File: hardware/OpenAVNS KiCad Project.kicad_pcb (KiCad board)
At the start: 4 copper layers, 69.9 x 100.9 mm, 210 parts, among them J1 Conn_ARM_JTAG_SWD_10, J2 AudioPlug3, J3 USB_C_Receptacle, J4 Conn_01x02_Pin, J5 Conn_01x03_Pin, Q1 BCV62, Q2 BC847, Q3 BC857, Q4 BCV61, Q5 BCV62, Q6 BC847, Q7 BC857, Q8 BCV61, SW1 SW_SPDT, T1 Wurth 750315839 - 1:10, 40uH, U1 TS5A3159AYZPR, U10 TLV9062, U11 LIS2DH12, U12 OPA455, U13 74AUC1G74, U14 TPS61200DRC, U15 LT1615ES5_TRPBF, U16 LT8304IS8E_PBF, U17 MCP73831-2-OT, U2 TLV9004xRUCR, U3 MCP4725xxx-xCH, U4 TS5A3159AYZPR, U5 nRF52840, U6 TS5A3159AYZPR, U7 MCP4725xxx-xCH, U8 TS5A3159AYZPR, U9 OPA455, Y1 32MHz - X322532MOB4SI

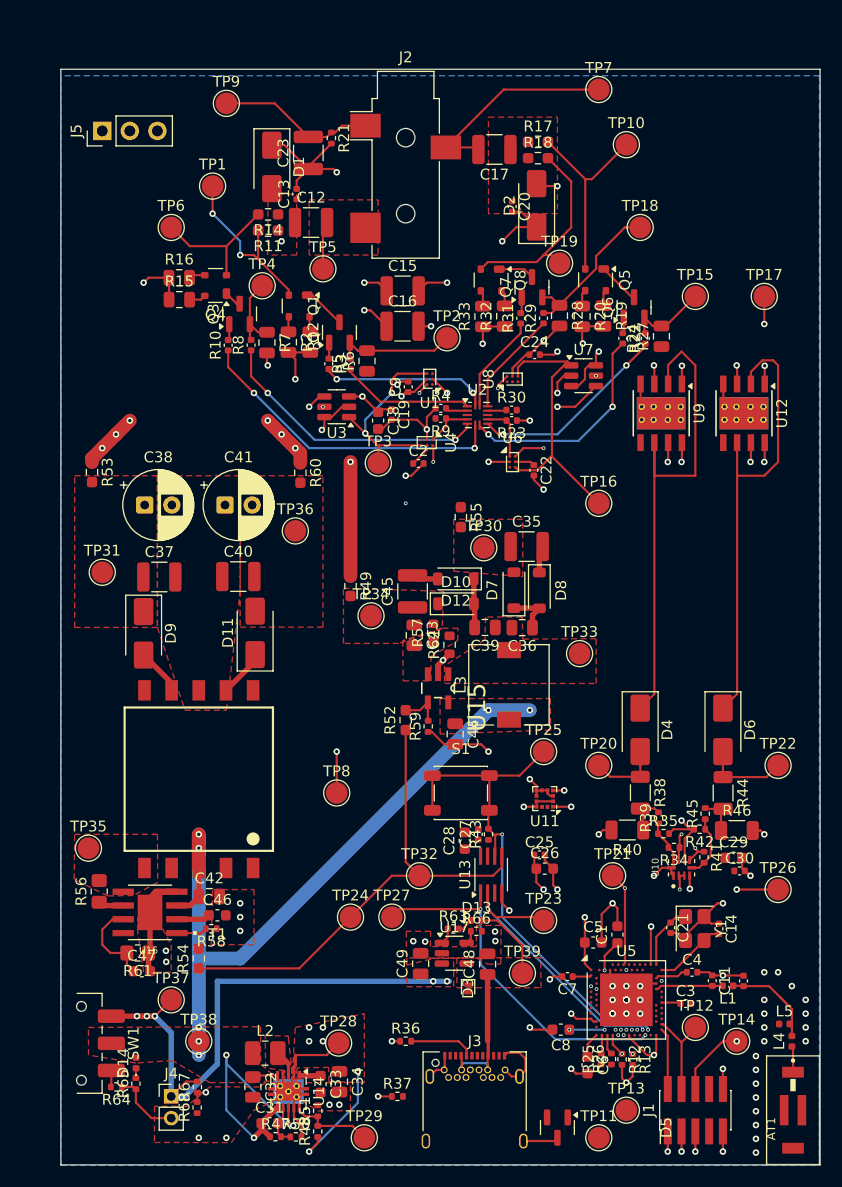
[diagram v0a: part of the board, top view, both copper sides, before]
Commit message: Added mounting holes
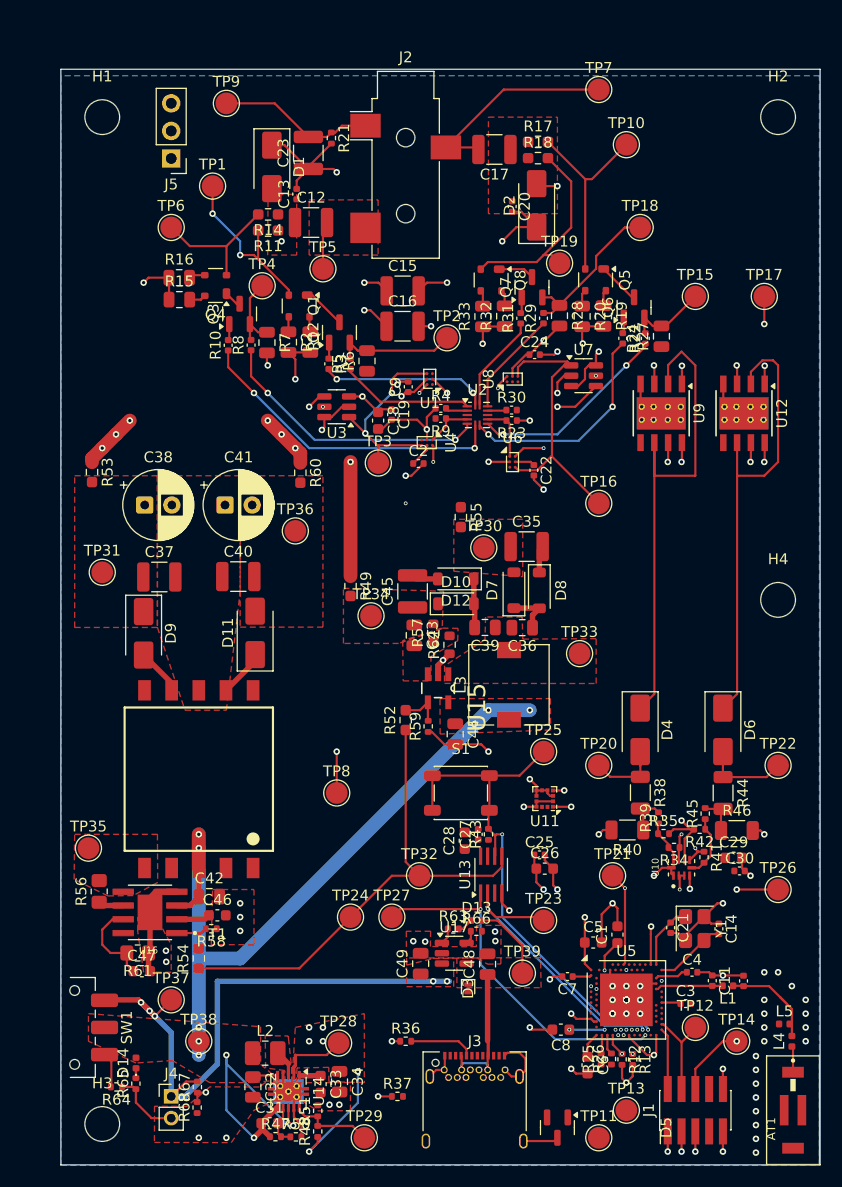
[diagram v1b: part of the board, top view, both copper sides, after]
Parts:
- added H1: MountingHole, MountingHole:MountingHole_3.2mm_M3_DIN965, F.Cu at (198.1, 64.8)
- added H2: MountingHole, MountingHole:MountingHole_3.2mm_M3_DIN965, F.Cu at (260.4, 64.8)
- added H3: MountingHole, MountingHole:MountingHole_3.2mm_M3_DIN965, F.Cu at (198.1, 157.5)
- added H4: MountingHole, MountingHole:MountingHole_3.2mm_M3_DIN965, F.Cu at (260.4, 109.2)
- moved J5 6.84 mm to (204.5, 68.6), turned to 180 degrees
- moved SW1 1.59 mm to (195.6, 148.6)
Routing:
- net /VBAT: track 53.2 -> 55.8 mm
- net Net-(SW1-C): track 1.53 -> 3.25 mm

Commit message: Finished routing, working through DRC
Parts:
- added G***: LOGO, LOGO, F.Cu at (115.6, 87.6)
- moved TP11 138.0 mm to (106.7, 143.5)
- moved R26 137.5 mm to (108.2, 137.2)
- moved R30 136.9 mm to (99.8, 75.6)
- moved D5 136.8 mm to (104.3, 141.1), turned to 0 degrees
- moved AT1 136.7 mm to (125.8, 141.0)
- moved C30 136.7 mm to (120.9, 118.9)
- moved H2 136.7 mm to (124.5, 49.5)
- moved H4 136.7 mm to (124.5, 94.0)
- moved TP22 136.7 mm to (124.5, 109.2)
- moved C1 136.7 mm to (109.7, 124.8)
- moved C10 136.7 mm to (121.3, 129.1)
- moved C11 136.7 mm to (118.4, 129.0)
- moved C18 136.7 mm to (87.6, 77.5)
- moved C21 136.7 mm to (114.6, 124.2)
- moved C22 136.7 mm to (102.0, 82.0)
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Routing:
- net +3.3V: track 77.3 -> 155.3 mm, vias 20 -> 26
- net /Batt_Measure: track 1.67 -> 45.1 mm, vias 2 -> 3
- net /E2: track 19.4 -> 49.7 mm, vias 0 -> 1
- net /USB_D-: track 0.00 -> 23.4 mm, vias 0 -> 1
- net /USB_D+: track 0.00 -> 22.0 mm, vias 0 -> 1
- net /E1: track 4.42 -> 23.4 mm, vias 0 -> 1
- net Net-(J1-~{RESET}): track 12.3 -> 27.6 mm, vias 2 -> 3
- net /-HV: track 20.2 -> 34.7 mm, vias 6 -> 7
- net GND: track 159.5 -> 172.8 mm, vias 75 -> 111
- net /V_USB: track 23.2 -> 31.8 mm, vias 0 -> 2
- net Net-(J3-CC2): track 0.00 -> 8.12 mm, vias 0 -> 1
- net Net-(J1-SWDIO/TMS): track 5.69 -> 11.8 mm
- net /Ground_Electrode: track 14.5 -> 19.6 mm
- net /MCU_D-: track 1.72 -> 4.90 mm
- net Net-(U2A-+): track 2.04 -> 4.76 mm
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- added copper zone on In2.Cu, net /V_USB
- added copper zone on In2.Cu, net GND
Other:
- board text added: "OpenAVNS V1.0 Github.com/OpenAVNS"
- board text removed: "Add Headers for Outputs Add hatches for hand soldered components After deciding stackup, need to go through and calculate all 50 Ohm lines (USB data and RF antenna)"

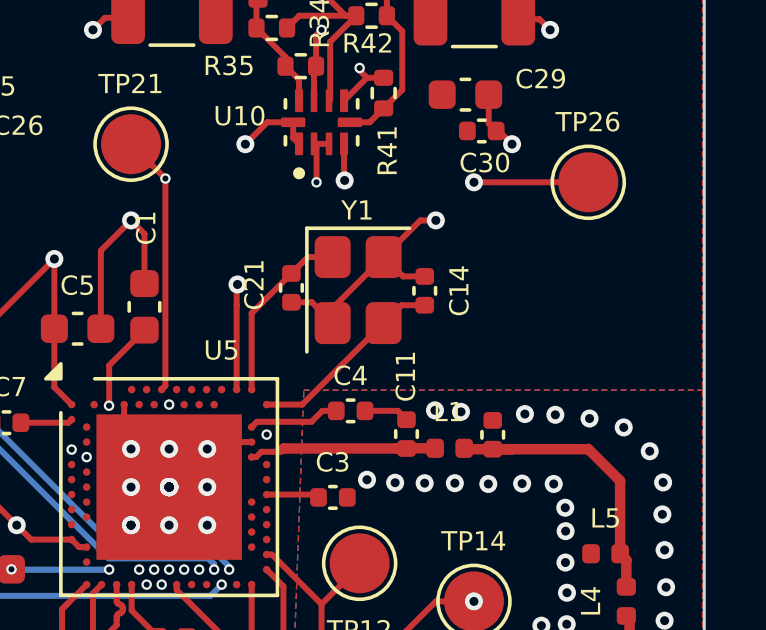
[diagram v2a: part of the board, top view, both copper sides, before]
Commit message: Added GPIO pin for triggering or other multipurpose applications
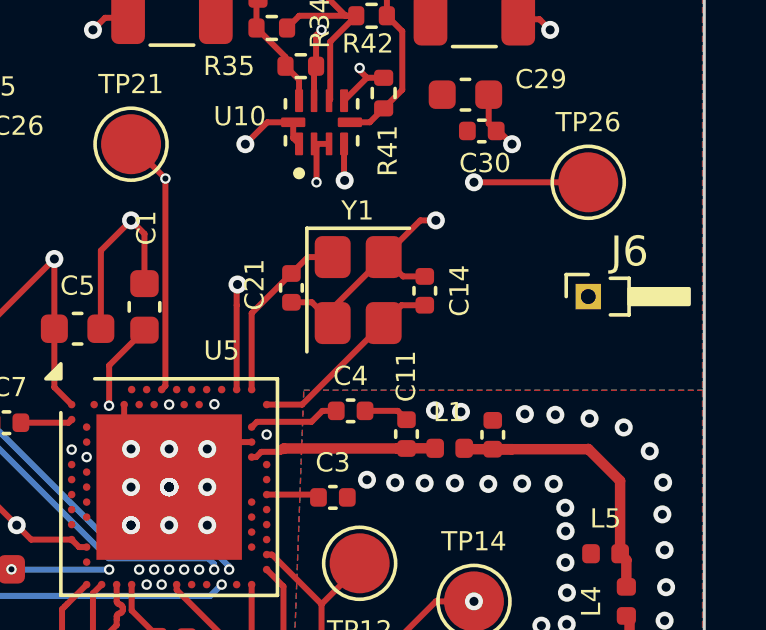
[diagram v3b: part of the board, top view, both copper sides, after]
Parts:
- added J6: Conn_01x01_Pin, Connector_PinHeader_1.00mm:PinHeader_1x01_P1.00mm_Horizontal, F.Cu at (124.5, 124.5)
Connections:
- U5 pad B19: unconnected-(U5-P1.11-PadB19) -> Net-(J6-Pin_1)
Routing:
- net Net-(J6-Pin_1): track 0.00 -> 13.9 mm, vias 0 -> 1
- net /Z2: track 23.5 -> 25.1 mm
